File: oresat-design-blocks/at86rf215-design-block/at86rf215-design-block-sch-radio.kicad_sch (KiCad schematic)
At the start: 43 parts, among them J1 SMA, J10 Conn_01x08, J11 Conn_01x05, J12 Conn_01x08, J2 USB4105-GF-A, J3 Conn_01x06, J6 Conn_01x06, J9 Screw_Terminal_01x02, SW1 RESET, U1 AT86RF215, U2 LP2985AIM5-1.8_NOPB, X1 TXETALSANF-26.000000

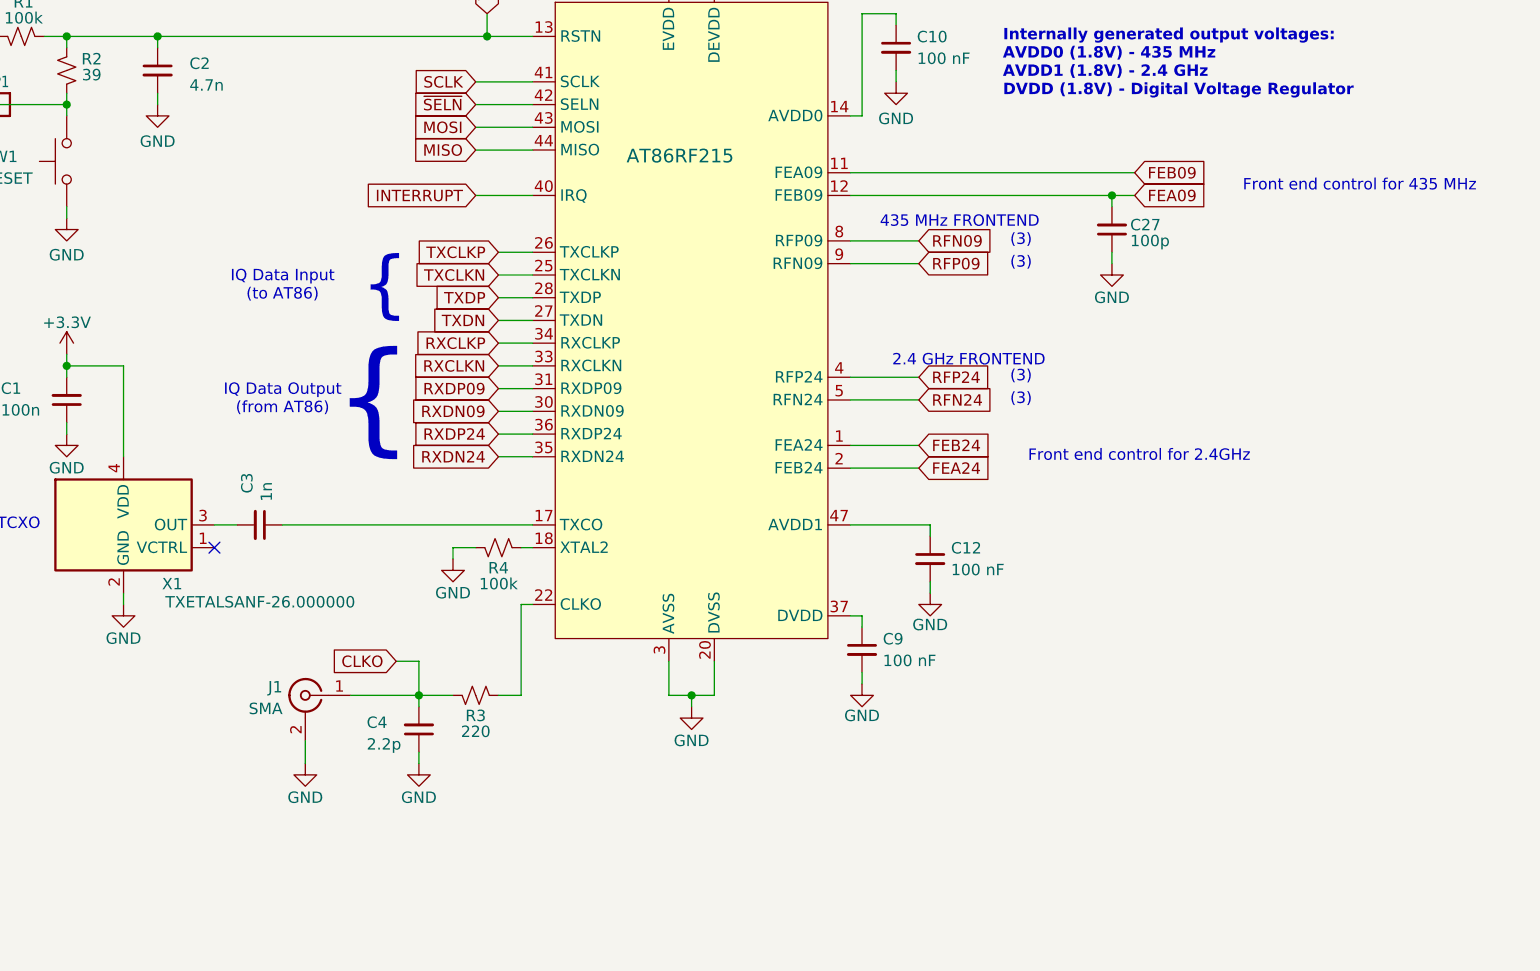
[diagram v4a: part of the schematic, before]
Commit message: Finish routing and silk screen layout, added ground stitching on border and RF lines
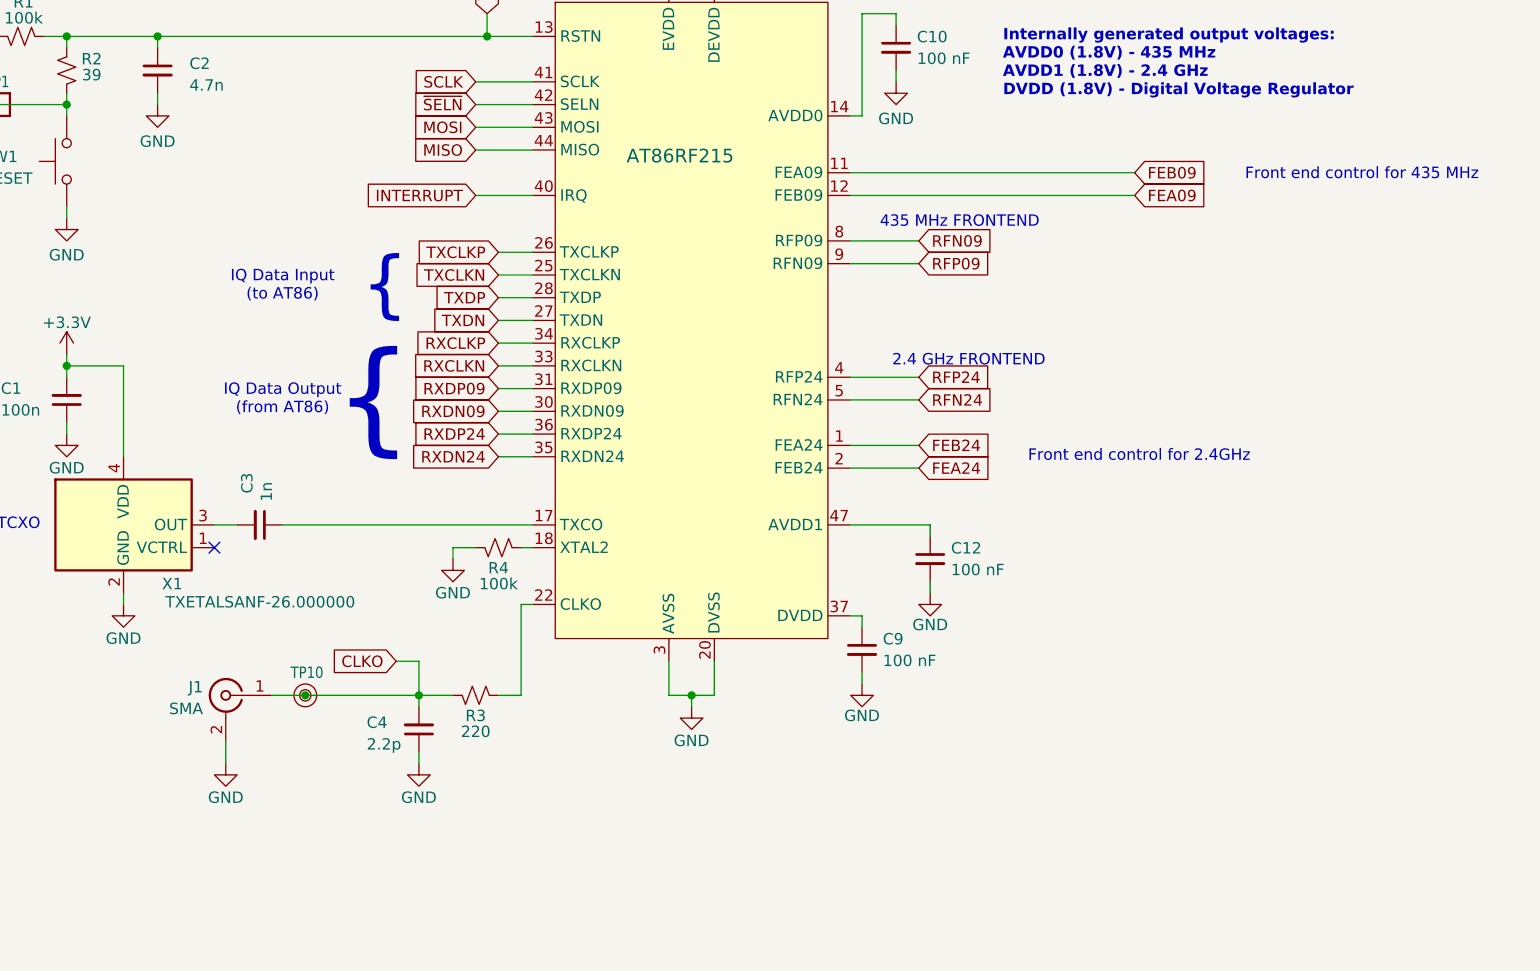
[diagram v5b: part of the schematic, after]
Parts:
- removed C27: 100p, oresat-passives:0402-C, symbol Device:C_Small
- added TP10: ~, oresat-misc:TestPoint_RF_Probe, symbol oresat-misc:Test-Point-RF-Probe-Stripline
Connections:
- net CLKO: now also TP10.1
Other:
- note removed: "(3)"
- moved on the sheet: J1

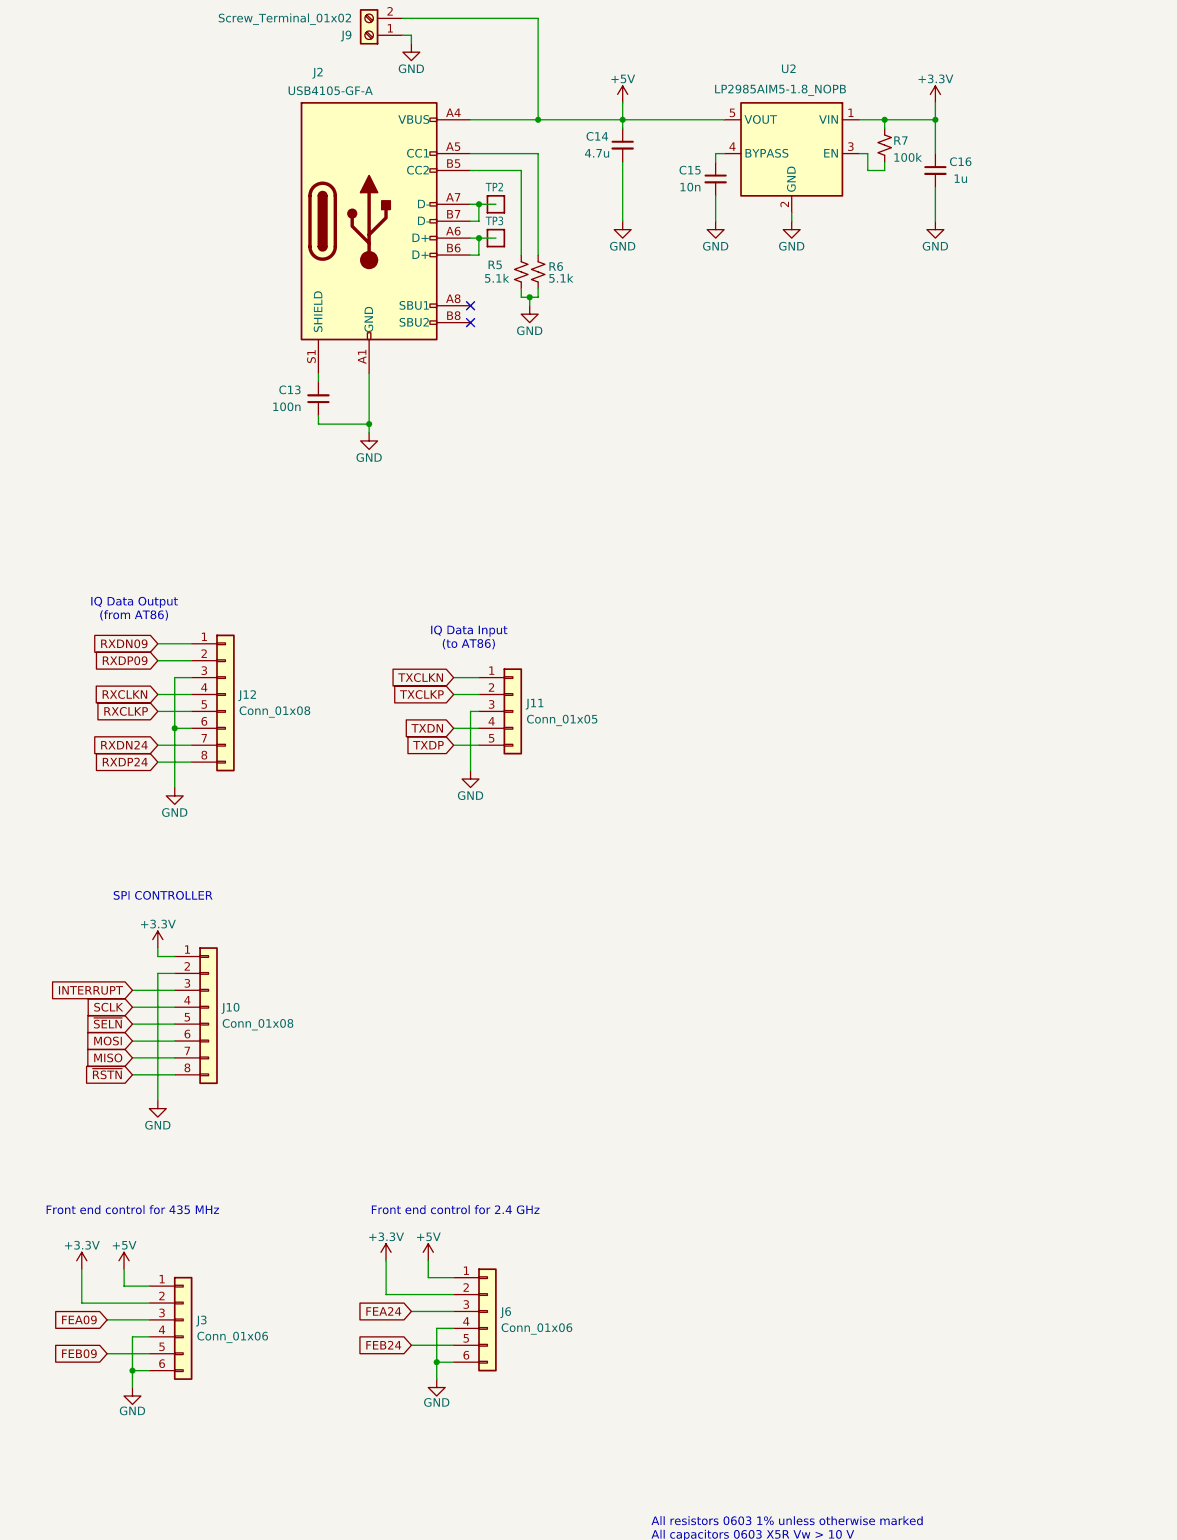
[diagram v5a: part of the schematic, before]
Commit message: Design review on AT86 breakout.
Added LEDs (you're welcome Theo), changed resistor values to be more matchy, deleted some unecessary grounds in layout, switching to 0603 and BOM still left.
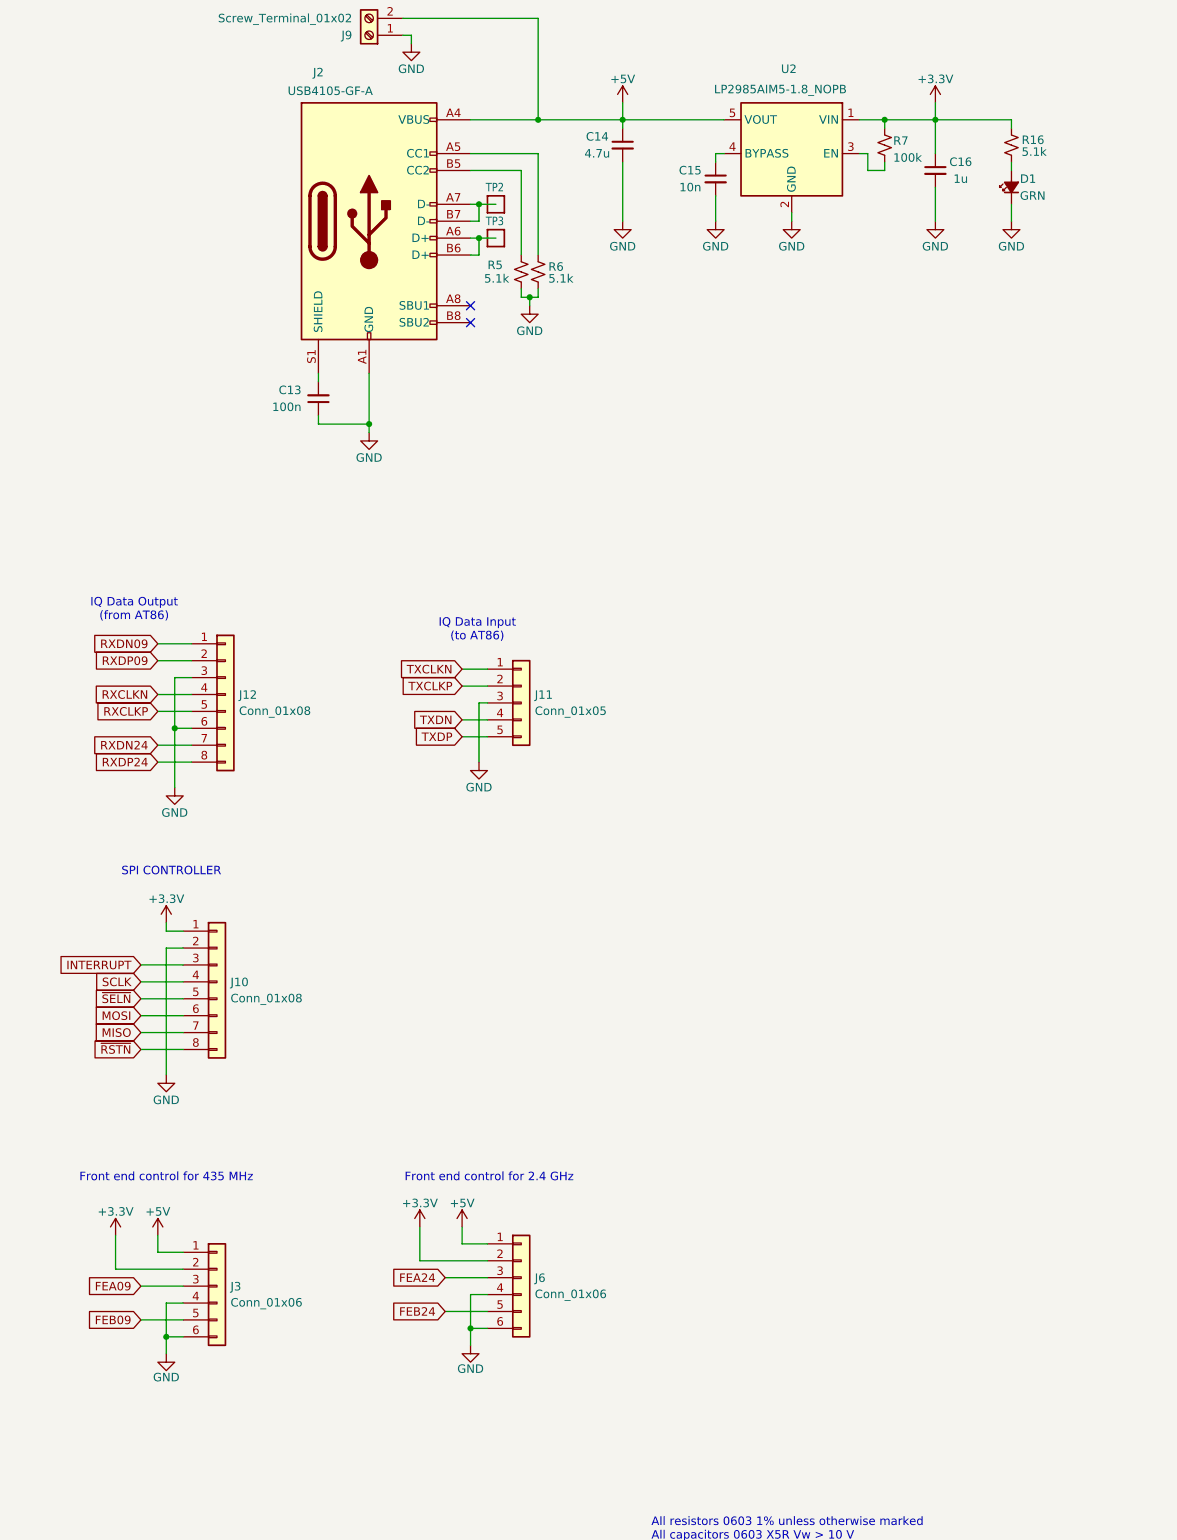
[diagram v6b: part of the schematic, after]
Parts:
- added D1: GRN, LED_SMD:LED_0603_1608Metric, symbol Device:LED_Small_Filled
- added R16: 5.1k, oresat-passives:0603-C-NOSILK, symbol Device:R_Small_US
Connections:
- net +3.3V: now also R16.1
- net AVSS: now also D1.1 (K)
- new net: D1.2 (A), R16.2
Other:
- moved on the sheet: J10, J11, J3, J6

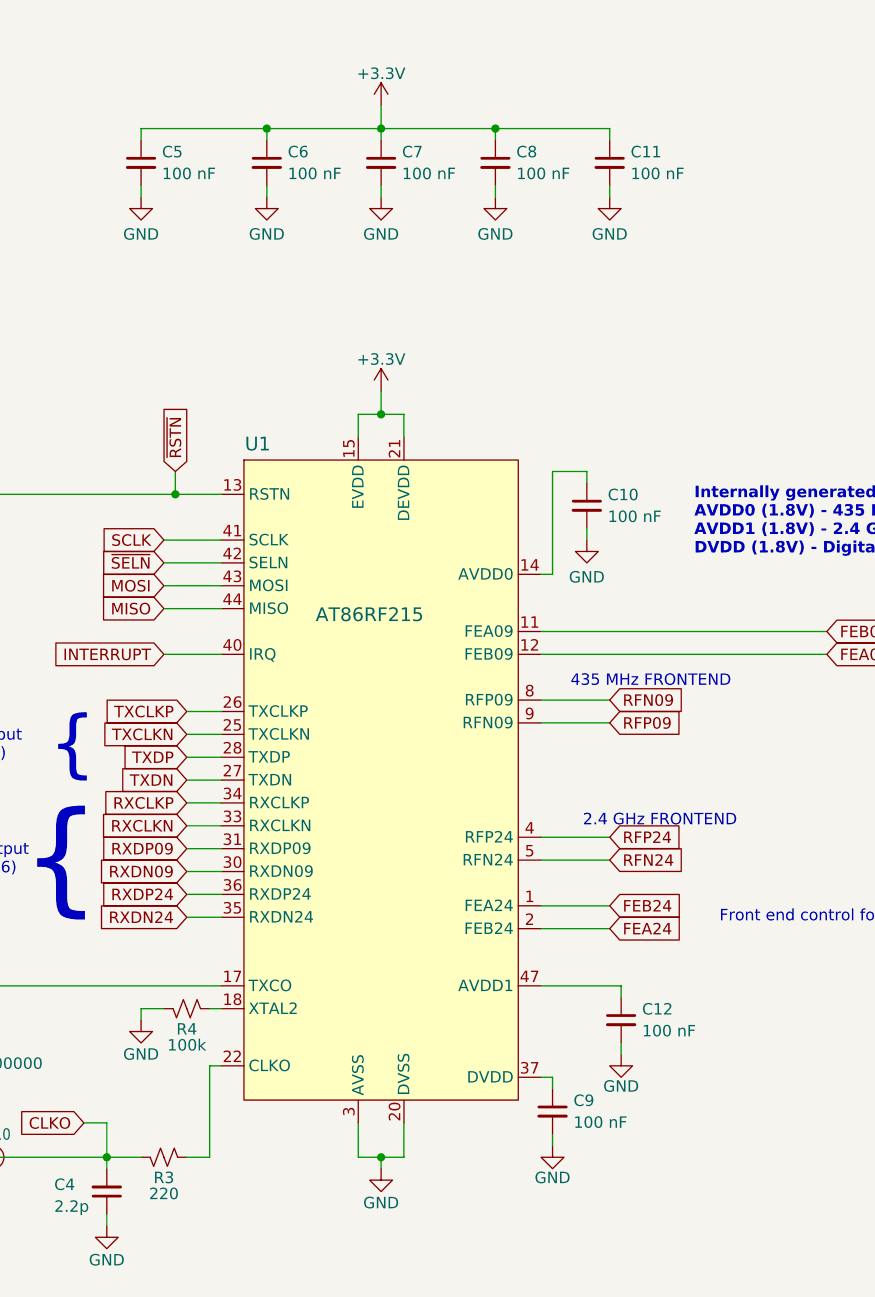
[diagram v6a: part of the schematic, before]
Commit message: swapped 0402 to 0603 and fixed layout, routed LEDs, fixed SMAs,  and fixed silkscreen
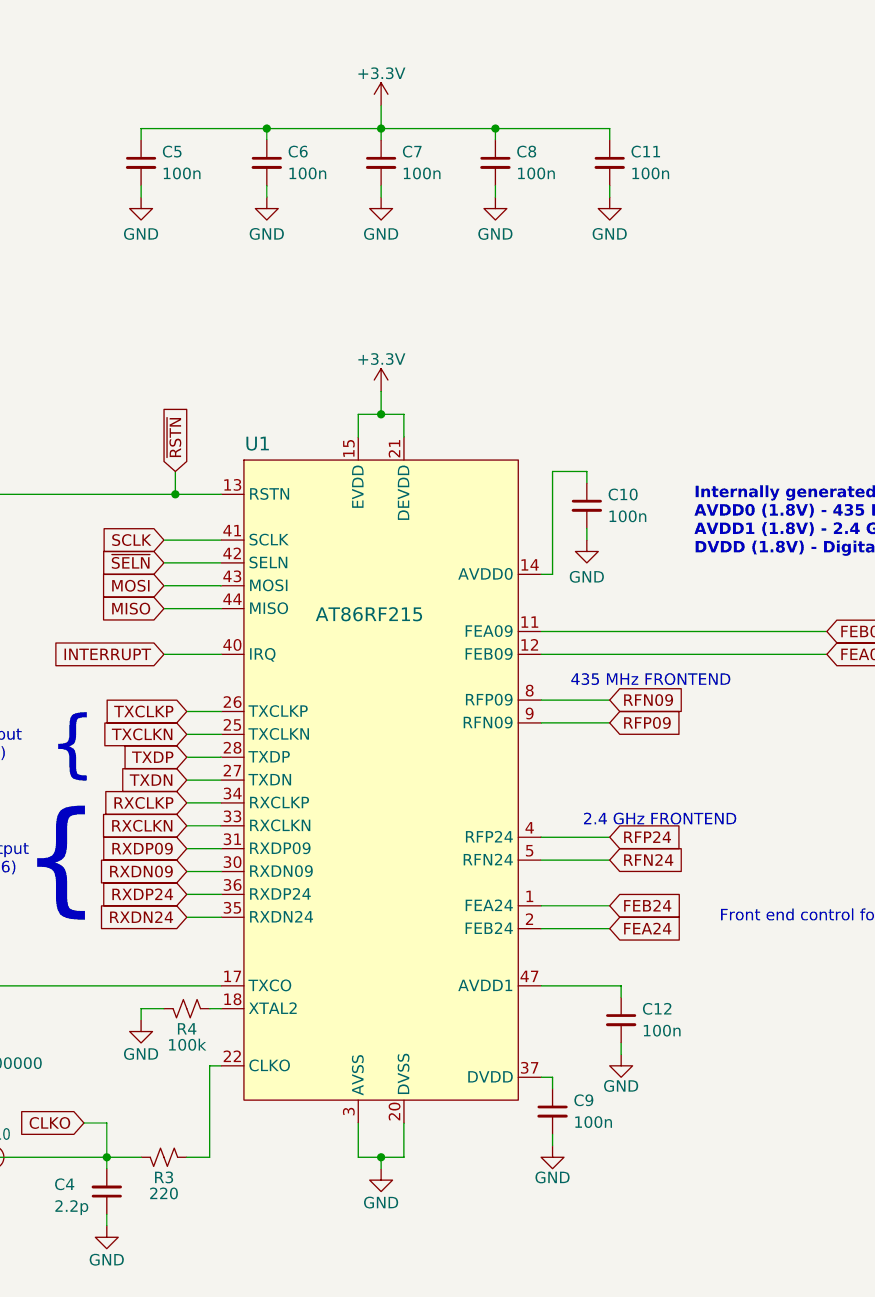
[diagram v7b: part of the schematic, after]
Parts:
- C1: footprint Capacitor_SMD:C_0603_1608Metric -> oresat-passives:0603-C-NOSILK; DIS (none) -> DigiKey; DPN (none) -> 587-3472-1-ND; MFR (none) -> Taiyo Yuden; MPN (none) -> TMK107BJ104KAHT
- C10, C11, C12, C5, C6, C7, C8, C9: value 100 nF -> 100n; footprint Capacitor_SMD:C_0603_1608Metric -> oresat-passives:0603-C-NOSILK; DIS (none) -> DigiKey; DPN (none) -> 587-3472-1-ND; MFR (none) -> Taiyo Yuden; MPN (none) -> TMK107BJ104KAHT
